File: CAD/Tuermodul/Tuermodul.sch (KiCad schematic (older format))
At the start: 52 parts, among them J101 Conn_02x16_Counter_Clockwise, U101 93LC46B, U102 74HC595, U103 FT4232H, U104 MCP1825S, Y101 12MHz

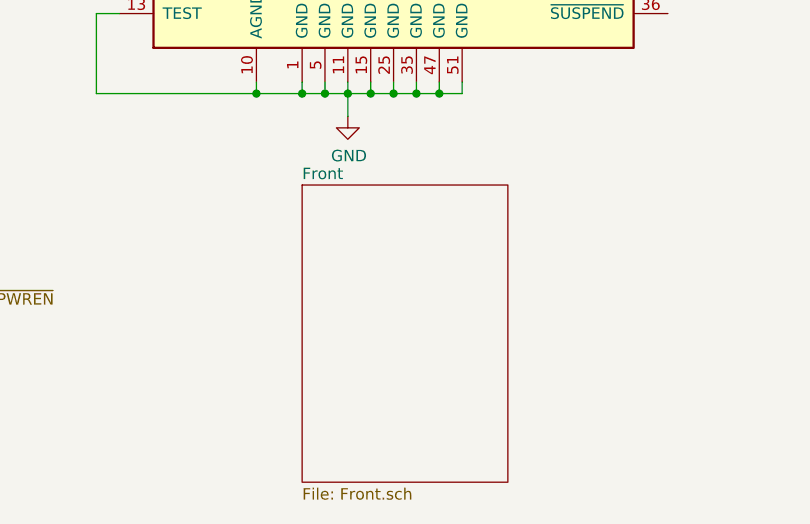
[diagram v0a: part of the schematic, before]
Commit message: -mod: Front und Hauptplatine separiert -mod: BOM von Nicolas überarbeitet
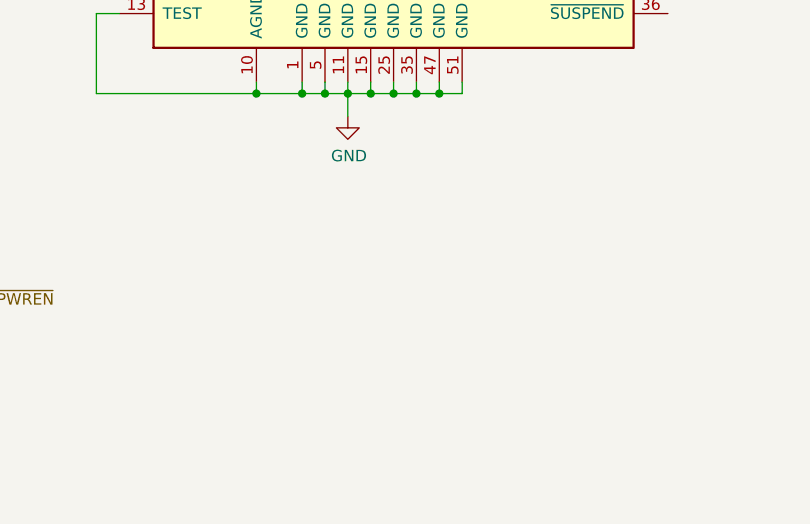
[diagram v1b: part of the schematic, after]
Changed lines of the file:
@@
 $Descr A4 11693 8268
 encoding utf-8
-Sheet 1 3
+Sheet 1 2
 Title ""
 Date ""
@@
 Wire Wire Line
 	2050 6950 1850 6950
-$Sheet
-S 5350 6350 900  1300
-U 5C54653F
-F0 "Front" 50
-F1 "Front.sch" 50
-$EndSheet
 $Comp
 L power:+3.3V #PWR0102
